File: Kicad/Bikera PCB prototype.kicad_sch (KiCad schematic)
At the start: 3 parts, among them U1 STM32L431CCTx, U2 RAK11720, U3 ATECC608B-SSHDA

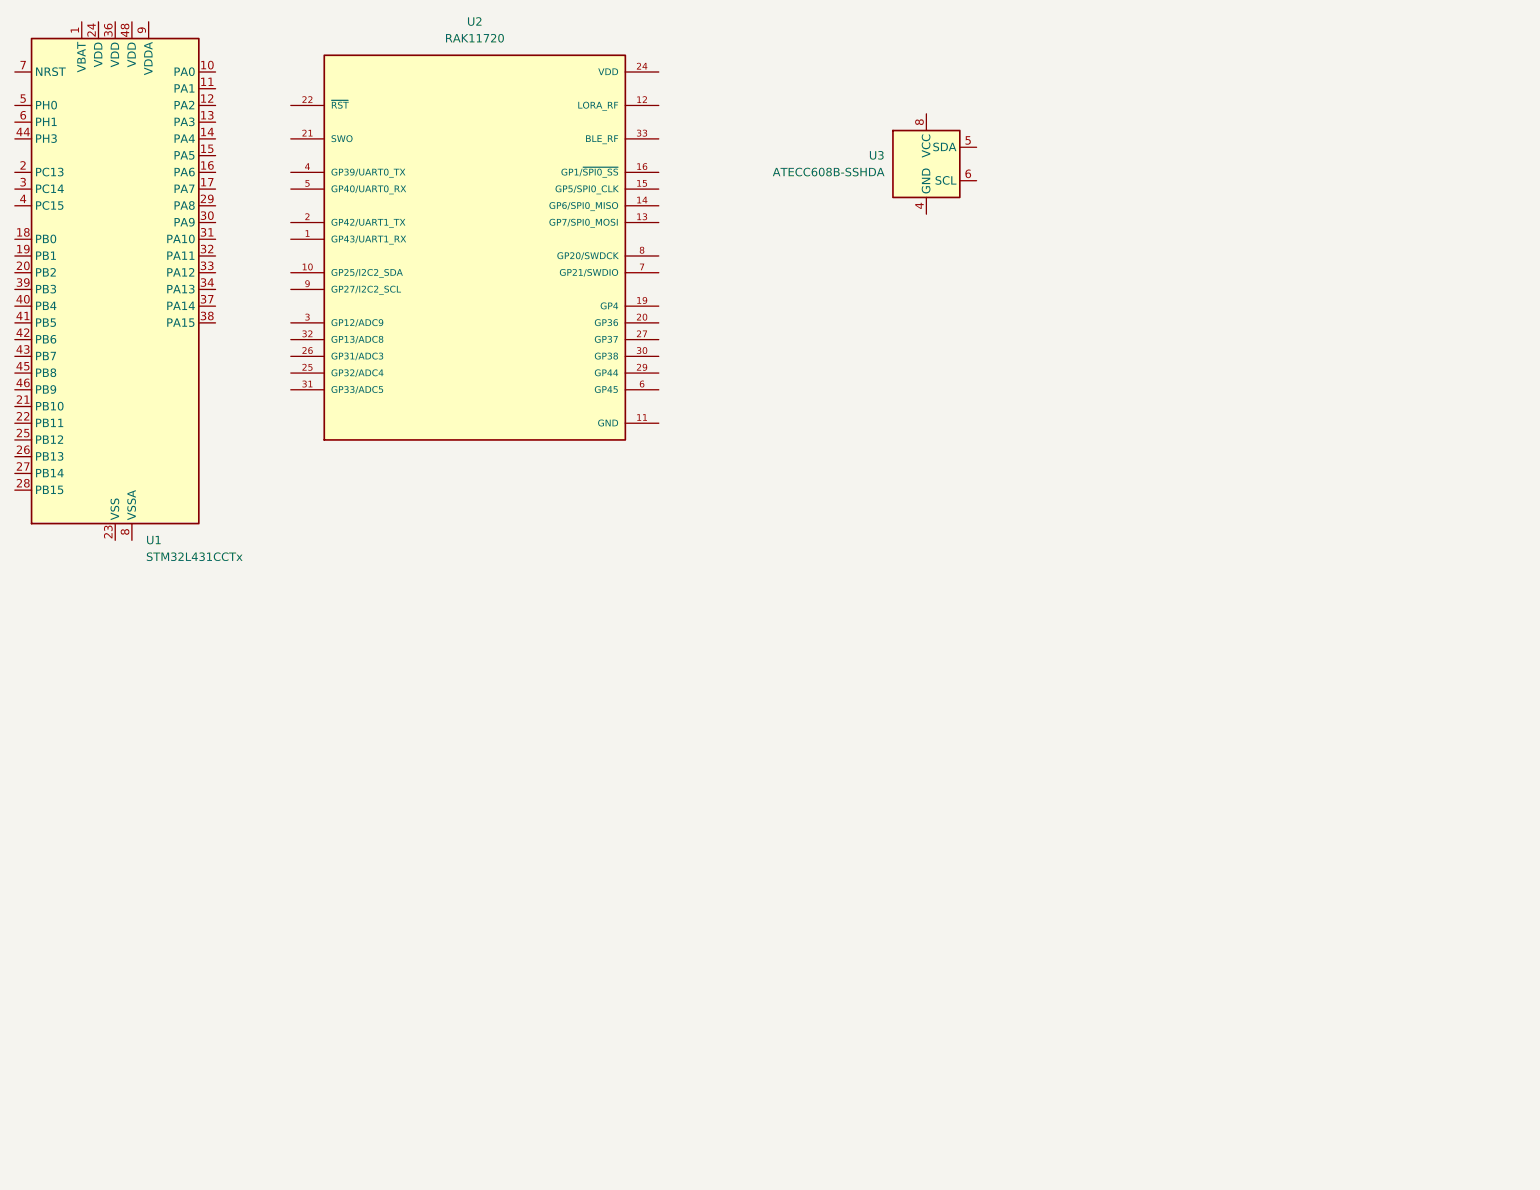
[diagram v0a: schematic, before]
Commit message: KiCad symbolen geïmporteerd
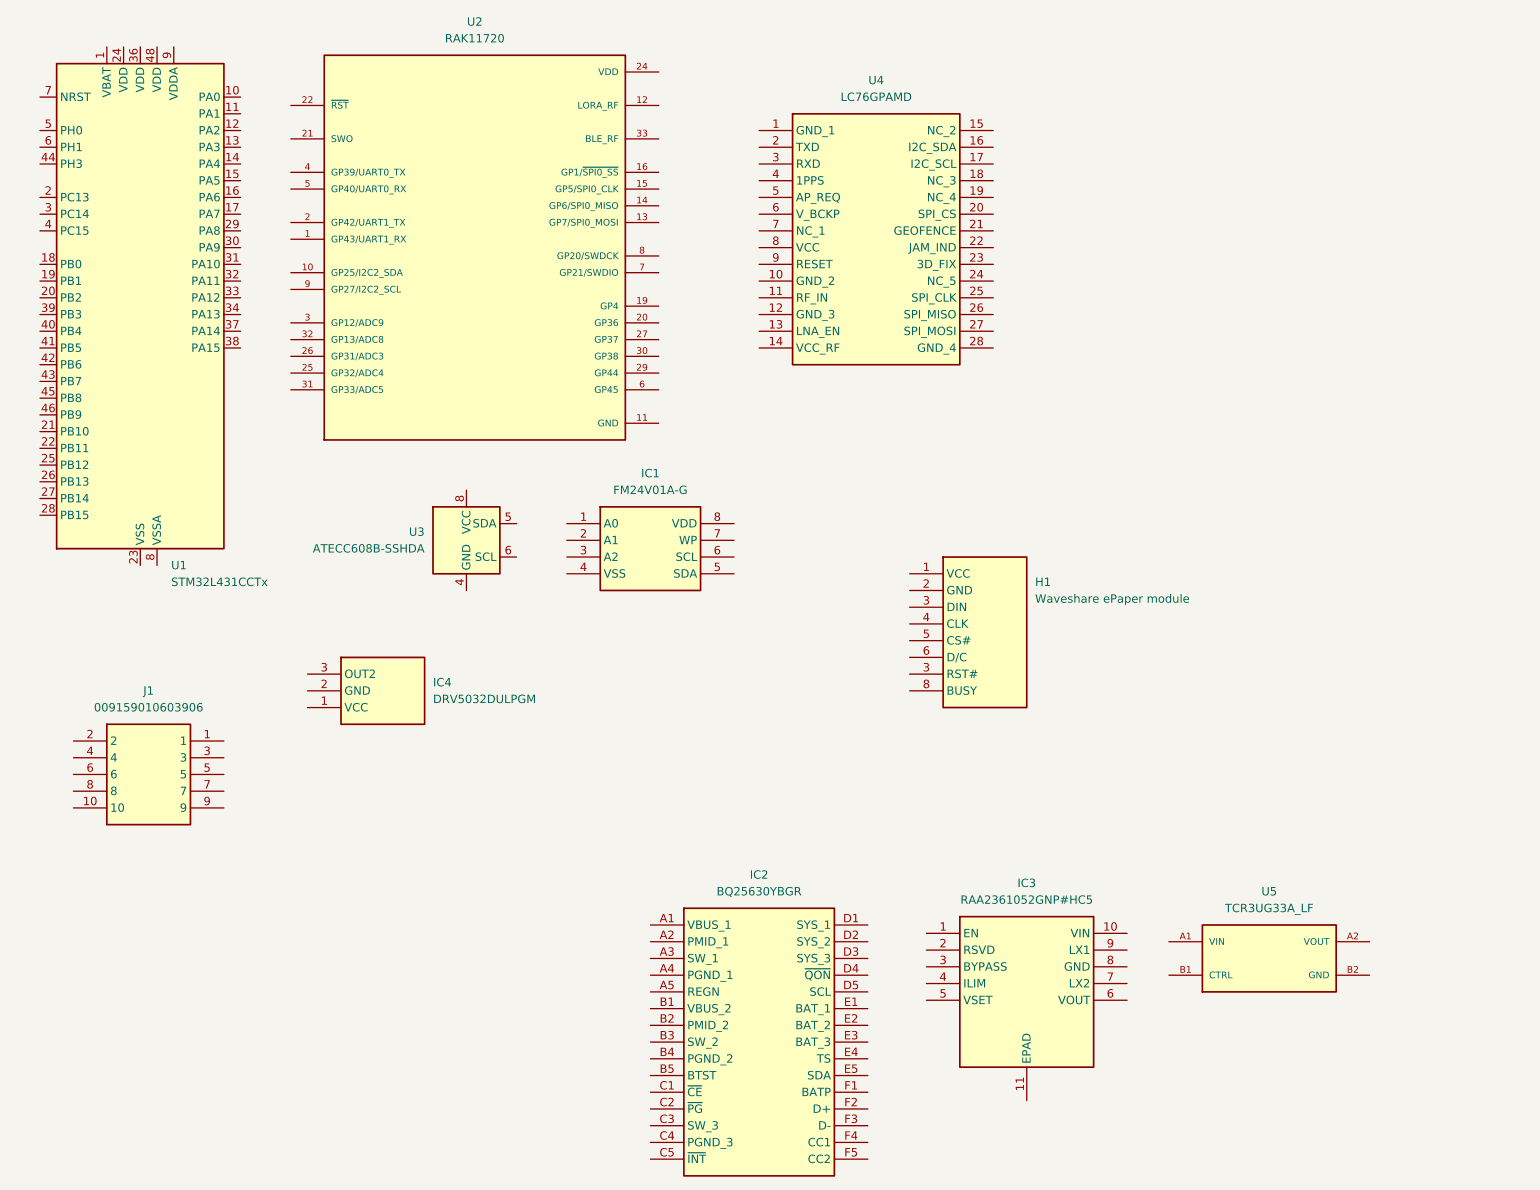
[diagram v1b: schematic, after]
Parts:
- added H1: Waveshare ePaper module, Connector_PinHeader_2.54mm:PinHeader_1x08_P2.54mm_Vertical, symbol Waveshare ePaper module:DRV5032DULPGM
- added IC1: FM24V01A-G, FM24V01A-G:SOIC127P602X173-8N, symbol FM24V01A-G:FM24V01A-G
- added IC2: BQ25630YBGR, BQ25630YBGR:BGA30C40P5X6_221X271X50, symbol BQ25630YBGR:BQ25630YBGR
- added IC3: RAA2361052GNP#HC5, RAA2361052GNP#HC5:SON50P250X250X90-11L-D, symbol RAA2361052GNP#HC5:RAA2361052GNP#HC5
- added IC4: DRV5032DULPGM, DRV5032DULPGM:DRV5032DULPGM, symbol DRV5032DULPGM:DRV5032DULPGM
- added J1: 009159010603906, 009159010603906:009159010603906, symbol 009159010603906:009159010603906
- added U4: LC76GPAMD, LC76GPAMD:LC76GPAMD, symbol LC76GPAMD:LC76GPAMD
- added U5: TCR3UG33A_LF, TCR3UG33A_LF:BGA4N35P2X2_64X64X33, symbol TCR3UG33A_LF:TCR3UG33A_LF
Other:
- moved on the sheet: U1, U3

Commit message: KiCad symbolen basiscomponenten
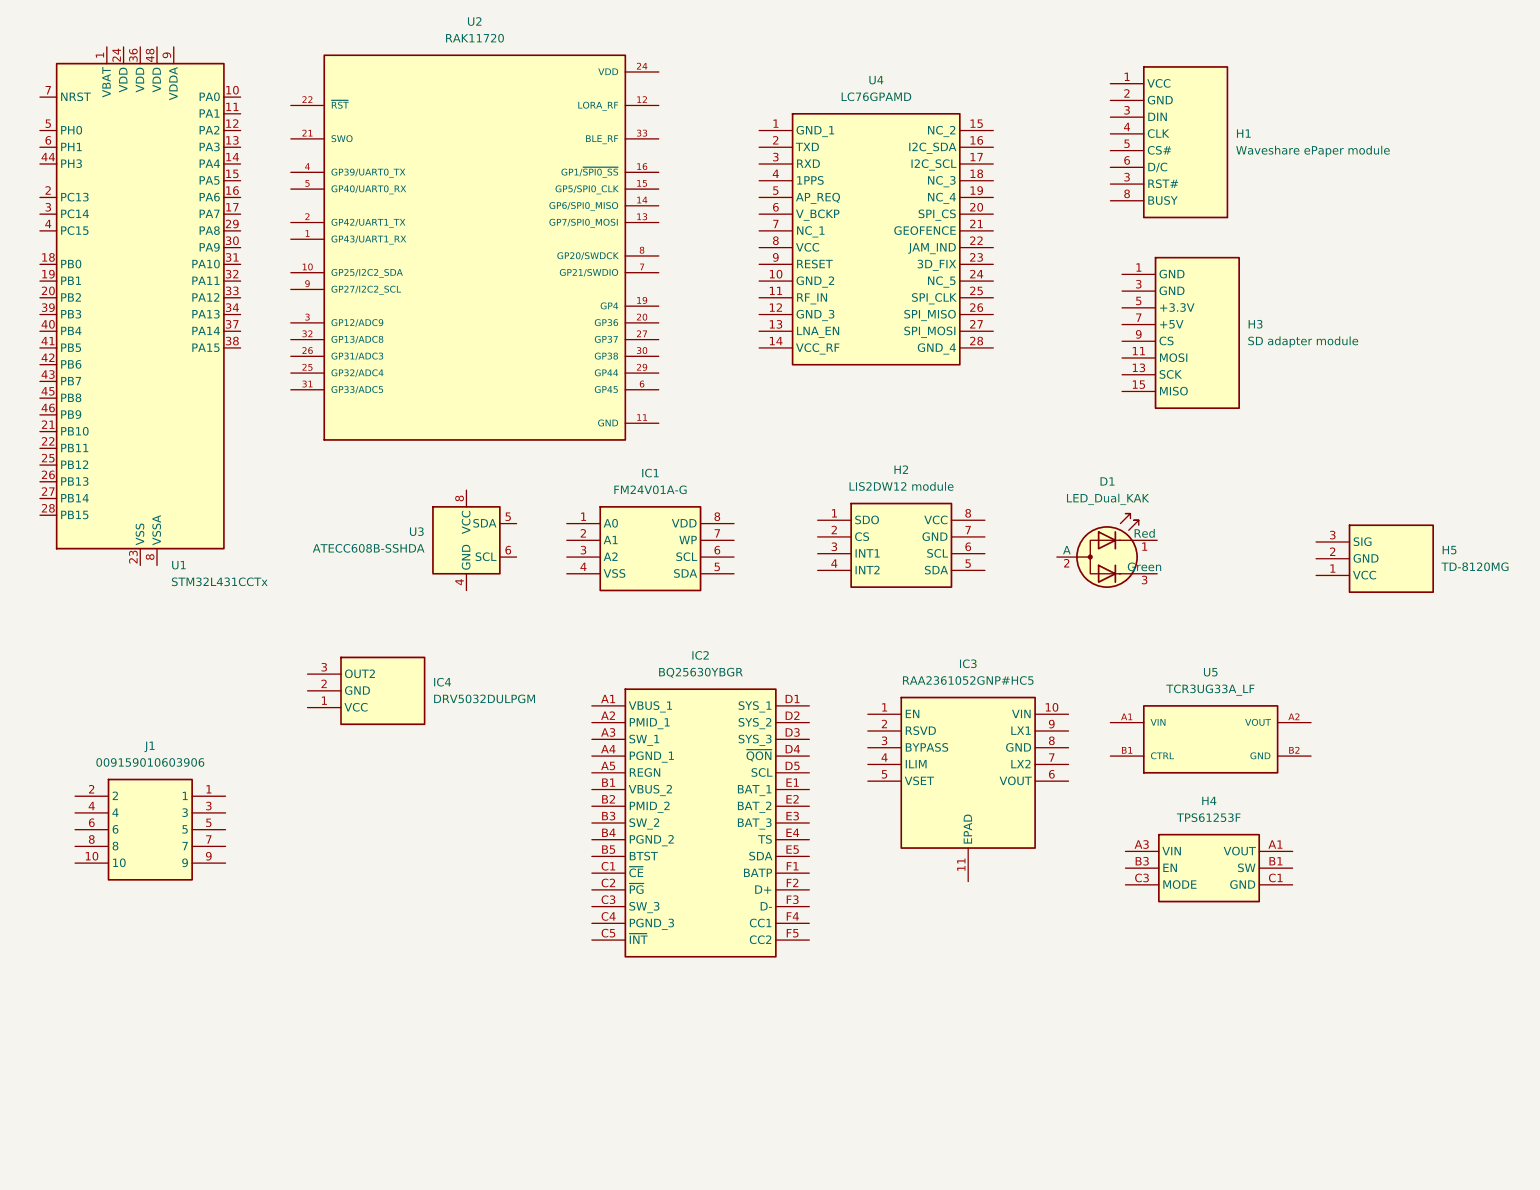
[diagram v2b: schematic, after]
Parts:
- removed H1: Waveshare ePaper module, Connector_PinHeader_2.54mm:PinHeader_1x08_P2.54mm_Vertical, symbol Waveshare ePaper module:DRV5032DULPGM
- added D1: LED_Dual_KAK, LED_THT:LED_D5.0mm-3, symbol Device:LED_Dual_KAK
- added H1: Waveshare ePaper module, Connector_PinHeader_2.54mm:PinHeader_1x08_P2.54mm_Vertical, symbol Waveshare ePaper module:Waveshare_ePaper_module
- added H2: LIS2DW12 module, symbol LIS2DW12:FM24V01A-G
- added H3: SD adapter module, Connector_PinHeader_2.54mm:PinHeader_2x08_P2.54mm_Horizontal, symbol SD adapter module:SD_adapter_module
- added H4: TPS61253F, TPS61253F:BGA9N40P3X3_119X128X62N, symbol TPS61253F:TPS61253F
- added H5: TD-8120MG, Connector_JST:JST_PH_B3B-PH-K_1x03_P2.00mm_Vertical, symbol TD-8120MG:TD-8120MG
- IC1: footprint FM24V01A-G:SOIC127P602X173-8N -> SOIC127P602X173-8N
- IC2: footprint BQ25630YBGR:BGA30C40P5X6_221X271X50 -> BGA30C40P5X6_221X271X50
- IC3: footprint RAA2361052GNP#HC5:SON50P250X250X90-11L-D -> SON50P250X250X90-11L-D
- IC4: footprint DRV5032DULPGM:DRV5032DULPGM -> DRV5032DULPGM
- J1: footprint 009159010603906:009159010603906 -> 009159010603906
- U4: footprint LC76GPAMD:LC76GPAMD -> LC76GPAMD
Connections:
- new net: H3.1 (GND), H3.2 (GND)
- new net: H3.10 (CS), H3.9 (CS)
- new net: H3.11 (MOSI), H3.12 (SCK)
- new net: H3.12 (SCK), H3.13 (SCK)
- new net: H3.14 (MISO), H3.15 (MISO)
- new net: H3.3 (GND), H3.4 (GND)
- new net: H4.A1 (VOUT), H4.A2 (VOUT)
- new net: H4.B1 (SW), H4.B2 (SW)
- new net: H4.C1 (GND), H4.C2 (GND)
- new net +3.3V: H3.5 (+3.3V), H3.6 (+3.3V)
- new net +5V: H3.7 (+5V), H3.8 (+5V)
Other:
- moved on the sheet: IC2, IC3, J1, U5
